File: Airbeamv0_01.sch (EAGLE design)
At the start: 86 parts

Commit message: did Dave's final updates
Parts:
- removed FAN_MOS-N1: DNP, Airbeam:MOSFET
- removed UC_F1: MH2029-300Y, wuerth-elektronik:WE-CBF_0805
- added CA_FB1: FERITE_BEAD, Airbeam:FERITE_BEAD
- added U$1: MOSFET-N, Airbeam:MOSFET-N
- U_FB1: value U_FB1 -> FERITE_BEAD; device wuerth-elektronik:WE-CBF_0805 -> Airbeam:FERITE_BEAD; PARTNO MH2029-300Y -> MH2029-300YCT-ND
- U_FB2: value U_FB2 -> FERITE_BEAD; device wuerth-elektronik:WE-CBF_0805 -> Airbeam:FERITE_BEAD; PARTNO MH2029-300Y -> MH2029-300YCT-ND
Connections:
- net +3V3: now also U$1.P$2; no longer FAN_MOS-N1.P$2
- net +5V: now also U_FB2.P$1; no longer UC_F1.1
- net AVCC: now also U_FB2.P$2; no longer UC_F1.2
- net D5*/FAN_CONTROL: now also U$1.P$1; no longer FAN_MOS-N1.P$1
- net GND: now also CA_FB1.P$1, U_FB1.P$1; no longer U_FB1.2, U_FB2.2
- net N$7: now also CA_FB1.P$2; no longer U_FB1.1
- net UGND: now also U_FB1.P$2; no longer U_FB2.1
- net VFAN: now also U$1.P$3; no longer FAN_MOS-N1.P$3
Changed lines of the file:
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@@
 <attribute name="PARTNO" value="CG0603MLC-05E"/>
-</part>
-<part name="U_FB2" library="wuerth-elektronik" deviceset="WE-CBF" device="_0805" value="U_FB2">
-<attribute name="PARTNO" value="MH2029-300Y"/>
 </part>
 <part name="U$25" library="MyPOW" deviceset="VUSB" device=""/>
 <part name="SUPPLY2" library="supply2" deviceset="GND1" device="" value="UGND"/>
-<part name="UC_F1" library="wuerth-elektronik" deviceset="WE-CBF" device="_0805" value="MH2029-300Y">
-<attribute name="PARTNO" value="MH2029-300Y"/>
-</part>
 <part name="UC_C2" library="SparkFun-Passives" deviceset="CAP" device="0603-CAP" value="100n">
 <attribute name="PARTNO" value="C1608X7R1E104K080AA"/>
@@
 <attribute name="PARTNO" value="RC0603JR-0710KL"/>
 </part>
-<part name="FAN_MOS-N1" library="Airbeam" deviceset="MOSFET" device="" value="DNP">
-<attribute name="PARTNO" value="IRLML2246TRPBF "/>
-</part>
 <part name="VR_R4" library="SparkFun-Resistors" deviceset="RESISTOR" device="0603" value="0">
 <attribute name="PARTNO" value="RC0603JR-070RL"/>
@@
 <attribute name="PARTNO" value="CG0603MLC-05E"/>
 </part>
-<part name="U_FB1" library="wuerth-elektronik" deviceset="WE-CBF" device="_0805" value="U_FB1">
-<attribute name="PARTNO" value="MH2029-300Y"/>
-</part>
 <part name="GND5" library="supply1" deviceset="GND" device=""/>
 <part name="DUST_SENSOR" library="Airbeam" deviceset="PART_OFFBOARD" device="" value="OFF_BOARD">
@@
 </part>
 <part name="GND47" library="supply1" deviceset="GND" device=""/>
+<part name="U_FB1" library="Airbeam" deviceset="FERITE_BEAD" device="">
+<attribute name="PARTNO" value="MH2029-300YCT-ND "/>
+</part>
+<part name="CA_FB1" library="Airbeam" deviceset="FERITE_BEAD" device="">
+<attribute name="PARTNO" value="MH2029-300YCT-ND "/>
+</part>
+<part name="U_FB2" library="Airbeam" deviceset="FERITE_BEAD" device="">
+<attribute name="PARTNO" value="MH2029-300YCT-ND "/>
+</part>
+<part name="U$1" library="Airbeam" deviceset="MOSFET-N" device=""/>
 </parts>
 <sheets>
@@
 <attribute name="PARTNO" x="-86.36" y="-68.58" size="1.778" layer="96" display="off"/>
 </instance>
-<instance part="U_FB2" gate="G$1" x="-129.54" y="-53.34" rot="R180">
-<attribute name="PARTNO" x="-129.54" y="-53.34" size="1.778" layer="96" display="off"/>
-</instance>
 <instance part="U$25" gate="G$1" x="-38.1" y="66.04"/>
 <instance part="SUPPLY2" gate="G$1" x="-53.34" y="38.1"/>
-<instance part="UC_F1" gate="G$1" x="-50.8" y="101.6">
-<attribute name="PARTNO" x="-50.8" y="101.6" size="1.778" layer="96" display="off"/>
-</instance>
 <instance part="UC_C2" gate="G$1" x="-40.64" y="134.62">
 <attribute name="PARTNO" x="-40.64" y="134.62" size="1.778" layer="96" display="off"/>
@@
 <attribute name="PARTNO" x="269.24" y="91.44" size="1.778" layer="96" rot="R180" display="off"/>
 </instance>
-<instance part="FAN_MOS-N1" gate="G$1" x="-96.52" y="-162.56" rot="R270">
-<attribute name="PARTNO" x="-96.52" y="-162.56" size="1.778" layer="96" rot="R270" display="off"/>
-</instance>
 <instance part="VR_R4" gate="G$1" x="-96.52" y="-172.72">
 <attribute name="PARTNO" x="-96.52" y="-172.72" size="1.778" layer="96" display="off"/>
@@
 <attribute name="PARTNO" x="-149.86" y="-205.74" size="1.778" layer="96" rot="R270" display="off"/>
 </instance>
-<instance part="U_FB1" gate="G$1" x="-149.86" y="-218.44" rot="R180">
-<attribute name="PARTNO" x="-149.86" y="-218.44" size="1.778" layer="96" display="off"/>
-</instance>
 <instance part="GND5" gate="1" x="-175.26" y="-193.04" rot="R270"/>
 <instance part="DUST_SENSOR" gate="G$1" x="238.76" y="-5.08">
@@
 </instance>
 <instance part="GND47" gate="1" x="119.38" y="-104.14"/>
+<instance part="U_FB1" gate="G$1" x="-129.54" y="-55.88" rot="R90">
+<attribute name="PARTNO" x="-129.54" y="-55.88" size="1.778" layer="96" rot="R90" display="off"/>
+</instance>
+<instance part="CA_FB1" gate="G$1" x="-149.86" y="-220.98" rot="R90">
+<attribute name="PARTNO" x="-149.86" y="-220.98" size="1.778" layer="96" rot="R90" display="off"/>
+</instance>
+<instance part="U_FB2" gate="G$1" x="-50.8" y="104.14" rot="R90">
+<attribute name="PARTNO" x="-50.8" y="104.14" size="1.778" layer="96" rot="R90" display="off"/>
+</instance>
+<instance part="U$1" gate="G$1" x="-96.52" y="-162.56" rot="R270"/>
 </instances>
 <busses>
@@
 <wire x1="-27.94" y1="106.68" x2="-58.42" y2="106.68" width="0.1524" layer="91"/>
 <wire x1="-58.42" y1="106.68" x2="-58.42" y2="104.14" width="0.1524" layer="91"/>
-<wire x1="-58.42" y1="104.14" x2="-55.88" y2="104.14" width="0.1524" layer="91"/>
 <wire x1="-58.42" y1="104.14" x2="-58.42" y2="101.6" width="0.1524" layer="91"/>
 <wire x1="-58.42" y1="101.6" x2="-27.94" y2="101.6" width="0.1524" layer="91"/>
@@
 <junction x="-27.94" y="127"/>
 <junction x="-58.42" y="104.14"/>
-<pinref part="UC_F1" gate="G$1" pin="1"/>
 <pinref part="U_MEGA32U-Q" gate="G$1" pin="UVCC"/>
 <pinref part="U_MEGA32U-Q" gate="G$1" pin="VCC"/>
@@
 <pinref part="UC_C8" gate="G$1" pin="1"/>
 <junction x="-15.24" y="127"/>
+<pinref part="U_FB2" gate="G$1" pin="P$1"/>
+<wire x1="-53.34" y1="104.14" x2="-58.42" y2="104.14" width="0.1524" layer="91"/>
 </segment>
 <segment>
@@
 <pinref part="BT_C2" gate="G$1" pin="1"/>
 <wire x1="38.1" y1="-134.62" x2="38.1" y2="-139.7" width="0.1524" layer="91"/>
+<junction x="38.1" y="-139.7"/>
 </segment>
 <segment>
@@
 <wire x1="-86.36" y1="-83.82" x2="-96.52" y2="-83.82" width="0.1524" layer="91"/>
 <wire x1="-86.36" y1="-73.66" x2="-86.36" y2="-83.82" width="0.1524" layer="91"/>
-<wire x1="-134.62" y1="-55.88" x2="-144.78" y2="-55.88" width="0.1524" layer="91"/>
+<wire x1="-132.08" y1="-55.88" x2="-144.78" y2="-55.88" width="0.1524" layer="91"/>
 <wire x1="-144.78" y1="-55.88" x2="-144.78" y2="-48.26" width="0.1524" layer="91"/>
 <wire x1="-144.78" y1="-48.26" x2="-144.78" y2="-40.64" width="0.1524" layer="91"/>
@@
 <label x="-142.24" y="-55.88" size="1.778" layer="95"/>
 <pinref part="U_Z1" gate="G$1" pin="2"/>
-<pinref part="U_FB2" gate="G$1" pin="2"/>
 <pinref part="U_Z2" gate="G$1" pin="2"/>
 <pinref part="GND2" gate="1" pin="GND"/>
@@
 <junction x="-127" y="-27.94"/>
 <junction x="-129.54" y="-27.94"/>
+<pinref part="U_FB1" gate="G$1" pin="P$1"/>
 </segment>
 <segment>
@@
 <pinref part="U_Z3" gate="G$1" pin="2"/>
 <wire x1="-167.64" y1="-167.64" x2="-154.94" y2="-167.64" width="0.1524" layer="91"/>
-<pinref part="U_FB1" gate="G$1" pin="2"/>
-<wire x1="-154.94" y1="-220.98" x2="-167.64" y2="-220.98" width="0.1524" layer="91"/>
+<wire x1="-152.4" y1="-220.98" x2="-167.64" y2="-220.98" width="0.1524" layer="91"/>
 <wire x1="-167.64" y1="-220.98" x2="-167.64" y2="-205.74" width="0.1524" layer="91"/>
 <pinref part="GND5" gate="1" pin="GND"/>
@@
 <junction x="-167.64" y="-180.34"/>
 <junction x="-167.64" y="-205.74"/>
+<pinref part="CA_FB1" gate="G$1" pin="P$1"/>
 </segment>
 <segment>
@@
 <pinref part="VR_R4" gate="G$1" pin="1"/>
 <wire x1="-101.6" y1="-172.72" x2="-101.6" y2="-162.56" width="0.1524" layer="91"/>
-<pinref part="FAN_MOS-N1" gate="G$1" pin="P$2"/>
 <wire x1="-101.6" y1="-162.56" x2="-99.06" y2="-162.56" width="0.1524" layer="91"/>
 <wire x1="-101.6" y1="-162.56" x2="-106.68" y2="-162.56" width="0.1524" layer="91"/>
@@
 <pinref part="+3V4" gate="G$1" pin="+3V3"/>
 <junction x="-101.6" y="-162.56"/>
+<pinref part="U$1" gate="G$1" pin="P$2"/>
 </segment>
 <segment>
@@
 </segment>
 <segment>
-<wire x1="-124.46" y1="-55.88" x2="-111.76" y2="-55.88" width="0.1524" layer="91"/>
+<wire x1="-127" y1="-55.88" x2="-111.76" y2="-55.88" width="0.1524" layer="91"/>
 <wire x1="-111.76" y1="-55.88" x2="-111.76" y2="-43.18" width="0.1524" layer="91"/>
 <junction x="-111.76" y="-55.88"/>
 <label x="-119.38" y="-55.88" size="1.778" layer="95"/>
-<pinref part="U_FB2" gate="G$1" pin="1"/>
 <pinref part="SUPPLY1" gate="G$1" pin="GND1"/>
 <pinref part="CON_USB" gate="G$1" pin="T5"/>
 <wire x1="-111.76" y1="-43.18" x2="-121.92" y2="-43.18" width="0.1524" layer="91"/>
+<pinref part="U_FB1" gate="G$1" pin="P$2"/>
 </segment>
 </net>
@@
 </segment>
 <segment>
-<pinref part="FAN_MOS-N1" gate="G$1" pin="P$1"/>
 <wire x1="-96.52" y1="-154.94" x2="-96.52" y2="-160.02" width="0.1524" layer="91"/>
 <label x="-96.52" y="-154.94" size="1.778" layer="95"/>
+<pinref part="U$1" gate="G$1" pin="P$1"/>
 </segment>
 <segment>
@@
 <net name="AVCC" class="0">
 <segment>
-<wire x1="-45.72" y1="104.14" x2="-40.64" y2="104.14" width="0.1524" layer="91"/>
+<wire x1="-48.26" y1="104.14" x2="-40.64" y2="104.14" width="0.1524" layer="91"/>
 <wire x1="-40.64" y1="104.14" x2="-12.7" y2="104.14" width="0.1524" layer="91"/>
 <wire x1="-12.7" y1="104.14" x2="-7.62" y2="104.14" width="0.1524" layer="91"/>
@@
 <junction x="-12.7" y="104.14"/>
 <label x="-40.64" y="104.14" size="1.778" layer="95"/>
-<pinref part="UC_F1" gate="G$1" pin="2"/>
 <pinref part="U_MEGA32U-Q" gate="G$1" pin="AVCC1"/>
 <pinref part="U_MEGA32U-Q" gate="G$1" pin="AVCC"/>
 <pinref part="UC_C5" gate="G$1" pin="1"/>
+<pinref part="U_FB2" gate="G$1" pin="P$2"/>
 </segment>
 <segment>
@@
 <net name="VFAN" class="0">
 <segment>
-<pinref part="FAN_MOS-N1" gate="G$1" pin="P$3"/>
 <wire x1="-93.98" y1="-162.56" x2="-91.44" y2="-162.56" width="0.1524" layer="91"/>
 <pinref part="VR_R4" gate="G$1" pin="2"/>
@@
 <pinref part="CON_FAN" gate="G$1" pin="VCC"/>
 <junction x="-91.44" y="-162.56"/>
+<pinref part="U$1" gate="G$1" pin="P$3"/>
 </segment>
 </net>
@@
 <pinref part="CON_ADDON" gate="G$1" pin="P$5"/>
 <wire x1="-121.92" y1="-144.78" x2="-121.92" y2="-220.98" width="0.1524" layer="91"/>
-<pinref part="U_FB1" gate="G$1" pin="1"/>
-<wire x1="-121.92" y1="-220.98" x2="-144.78" y2="-220.98" width="0.1524" layer="91"/>
-</segment>
-</net>
+<wire x1="-121.92" y1="-220.98" x2="-147.32" y2="-220.98" width="0.1524" layer="91"/>
+<pinref part="CA_FB1" gate="G$1" pin="P$2"/>
+</segment>
+</net>

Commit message: updated per email
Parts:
- removed U_FUSE: 1.8A, SparkFun-PowerIC:PTCSMD-W
- added U_C3: 10uF, SparkFun-Passives:CAP0805
- added U_C4: 100nF, SparkFun-Passives:CAP0603-CAP
- added U_ILIM: USB-OVERCURRENT, Airbeam:USB-OVERCURRENT
- added U_R3: 10k, SparkFun-Passives:RESISTOR0603-RES
- added VR_C1: DNP, Airbeam:CAP_POL120UF
- added VR_FUSE: PTCSMD-W, SparkFun-PowerIC:PTCSMD-W
- VR_D1: value DIODE -> DIODESOD123; device Airbeam:DIODE -> Airbeam:DIODESOD123
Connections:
- new net N$5: VR_FUSE.1, VR_MOS-P1.P$3, VR_R3.2
- new net N$8: U_ILIM.FLG, U_R3.1
- net GND: now also VR_C1.-
- net UGND: now also U_C3.2, U_C4.2, U_ILIM.EN, U_ILIM.GND
- net VREG_IN: now also VR_C1.+, VR_FUSE.2; no longer VR_MOS-P1.P$3, VR_R3.2
- net VUSB: now also U_ILIM.OUT1, U_ILIM.OUT2, U_R3.2; no longer U_FUSE.2
- net XUSB: now also U_C3.1, U_C4.1, U_ILIM.IN1, U_ILIM.IN2; no longer U_FUSE.1
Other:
- moved on the sheet: 3_3V_FAN_COPOL, CON_BAT, DUST_SENSOR, LED_CH, LION_BATTERY, R_LED_CH, UR_C1, UR_R2, U_C1, U_C2, U_VR3, U_VR5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

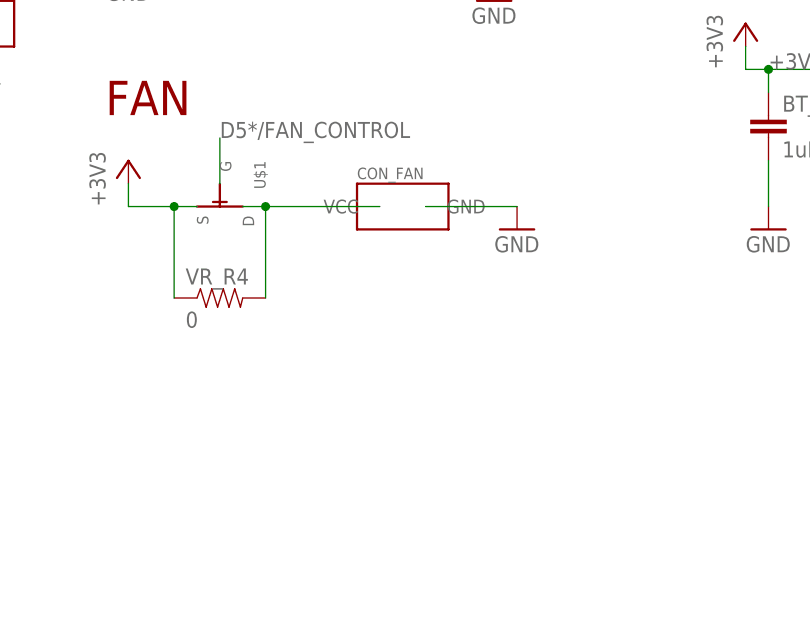
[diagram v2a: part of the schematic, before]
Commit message: added fan connector
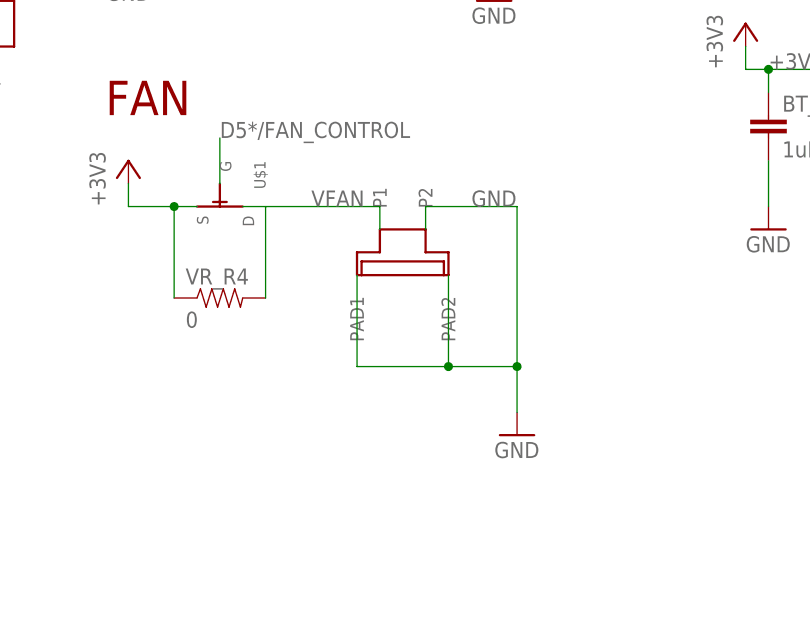
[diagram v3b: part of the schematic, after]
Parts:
- removed CON_FAN: FAN, Airbeam:FAN
- added U$2: SUR_2PIN, Airbeam:SUR_2PIN
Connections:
- net GND: now also U$2.P2, U$2.PAD1, U$2.PAD2; no longer CON_FAN.GND
- net VFAN: now also U$2.P1; no longer CON_FAN.VCC
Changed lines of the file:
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@@
 </part>
 <part name="+3V4" library="supply1" deviceset="+3V3" device=""/>
-<part name="CON_FAN" library="Airbeam" deviceset="FAN" device="">
-<attribute name="PARTNO" value="22-05-7025"/>
-</part>
 <part name="GND14" library="supply1" deviceset="GND" device=""/>
 <part name="R_LED_BT" library="SparkFun-Passives" deviceset="RESISTOR" device="0603-RES" value="1.4k">
@@
 <part name="GND48" library="supply1" deviceset="GND" device=""/>
 <part name="VR_FUSE" library="SparkFun-PowerIC" deviceset="PTC" device="SMD-W"/>
+<part name="U$2" library="Airbeam" deviceset="SUR_2PIN" device=""/>
 </parts>
 <sheets>
@@
 </instance>
 <instance part="+3V4" gate="G$1" x="-106.68" y="-157.48"/>
-<instance part="CON_FAN" gate="G$1" x="-76.2" y="-162.56">
-<attribute name="PARTNO" x="-76.2" y="-162.56" size="1.778" layer="96" display="off"/>
-</instance>
-<instance part="GND14" gate="1" x="-63.5" y="-165.1"/>
+<instance part="GND14" gate="1" x="-63.5" y="-187.96"/>
 <instance part="R_LED_BT" gate="G$1" x="76.2" y="-134.62" rot="R90">
 <attribute name="PARTNO" x="76.2" y="-134.62" size="1.778" layer="96" rot="R90" display="off"/>
@@
 <instance part="GND48" gate="1" x="147.32" y="-33.02"/>
 <instance part="VR_FUSE" gate="G$1" x="104.14" y="-22.86"/>
+<instance part="U$2" gate="G$1" x="-76.2" y="-167.64"/>
 </instances>
 <busses>
@@
 </segment>
 <segment>
-<pinref part="CON_FAN" gate="G$1" pin="GND"/>
-<wire x1="-73.66" y1="-162.56" x2="-63.5" y2="-162.56" width="0.1524" layer="91"/>
-<pinref part="GND14" gate="1" pin="GND"/>
-</segment>
-<segment>
 <pinref part="UBT" gate="G$1" pin="P$2"/>
 <wire x1="-15.24" y1="-121.92" x2="-30.48" y2="-121.92" width="0.1524" layer="91"/>
@@
 <wire x1="147.32" y1="-27.94" x2="147.32" y2="-30.48" width="0.1524" layer="91"/>
 <pinref part="GND48" gate="1" pin="GND"/>
+</segment>
+<segment>
+<pinref part="U$2" gate="G$1" pin="P2"/>
+<pinref part="GND14" gate="1" pin="GND"/>
+<wire x1="-73.66" y1="-165.1" x2="-73.66" y2="-162.56" width="0.1524" layer="91"/>
+<wire x1="-73.66" y1="-162.56" x2="-63.5" y2="-162.56" width="0.1524" layer="91"/>
+<wire x1="-63.5" y1="-162.56" x2="-63.5" y2="-180.34" width="0.1524" layer="91"/>
+<pinref part="U$2" gate="G$1" pin="PAD1"/>
+<wire x1="-63.5" y1="-180.34" x2="-63.5" y2="-185.42" width="0.1524" layer="91"/>
+<wire x1="-81.28" y1="-170.18" x2="-81.28" y2="-180.34" width="0.1524" layer="91"/>
+<wire x1="-81.28" y1="-180.34" x2="-71.12" y2="-180.34" width="0.1524" layer="91"/>
+<pinref part="U$2" gate="G$1" pin="PAD2"/>
+<wire x1="-71.12" y1="-180.34" x2="-71.12" y2="-170.18" width="0.1524" layer="91"/>
+<wire x1="-71.12" y1="-180.34" x2="-63.5" y2="-180.34" width="0.1524" layer="91"/>
+<junction x="-71.12" y="-180.34"/>
+<junction x="-63.5" y="-180.34"/>
+<label x="-68.58" y="-162.56" size="1.778" layer="95"/>
 </segment>
 </net>
@@
 <pinref part="VR_R4" gate="G$1" pin="2"/>
 <wire x1="-91.44" y1="-162.56" x2="-91.44" y2="-172.72" width="0.1524" layer="91"/>
+<pinref part="U$1" gate="G$1" pin="P$3"/>
+<pinref part="U$2" gate="G$1" pin="P1"/>
 <wire x1="-91.44" y1="-162.56" x2="-78.74" y2="-162.56" width="0.1524" layer="91"/>
-<pinref part="CON_FAN" gate="G$1" pin="VCC"/>
-<junction x="-91.44" y="-162.56"/>
-<pinref part="U$1" gate="G$1" pin="P$3"/>
-</segment>
-</net>
+<wire x1="-78.74" y1="-162.56" x2="-78.74" y2="-165.1" width="0.1524" layer="91"/>
+<label x="-86.36" y="-162.56" size="1.778" layer="95"/>
+</segment>
+</net>

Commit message: Final version! We are ordering this one!
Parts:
- CA_FB1, U_FB1, U_FB2: PARTNO MH2029-300YCT-ND -> MH2029-300Y
- CON_ADDON: PARTNO PPTC051LGBN-RC -> 950505-5002-AR
- VR_FUSE: value PTCSMD-W -> 1A; PARTNO (none) -> 0ZCJ0100FF2E
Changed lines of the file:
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@@
 <part name="GND17" library="supply1" deviceset="GND" device=""/>
 <part name="CON_ADDON" library="Airbeam" deviceset="CON_1X5" device="2MM">
-<attribute name="PARTNO" value="PPTC051LGBN-RC "/>
+<attribute name="PARTNO" value="950505-5002-AR"/>
 </part>
 <part name="P+5" library="supply1" deviceset="+5V" device=""/>
@@
 <part name="GND47" library="supply1" deviceset="GND" device=""/>
 <part name="U_FB1" library="Airbeam" deviceset="FERITE_BEAD" device="">
-<attribute name="PARTNO" value="MH2029-300YCT-ND "/>
+<attribute name="PARTNO" value="MH2029-300Y"/>
 </part>
 <part name="CA_FB1" library="Airbeam" deviceset="FERITE_BEAD" device="">
-<attribute name="PARTNO" value="MH2029-300YCT-ND "/>
+<attribute name="PARTNO" value="MH2029-300Y"/>
 </part>
 <part name="U_FB2" library="Airbeam" deviceset="FERITE_BEAD" device="">
-<attribute name="PARTNO" value="MH2029-300YCT-ND "/>
+<attribute name="PARTNO" value="MH2029-300Y"/>
 </part>
 <part name="U$1" library="Airbeam" deviceset="MOSFET-N" device=""/>
@@
 <part name="VR_C1" library="Airbeam" deviceset="CAP_POL" device="120UF" value="DNP"/>
 <part name="GND48" library="supply1" deviceset="GND" device=""/>
-<part name="VR_FUSE" library="SparkFun-PowerIC" deviceset="PTC" device="SMD-W"/>
+<part name="VR_FUSE" library="SparkFun-PowerIC" deviceset="PTC" device="SMD-W" value="1A">
+<attribute name="PARTNO" value="0ZCJ0100FF2E"/>
+</part>
 <part name="U$2" library="Airbeam" deviceset="SUR_2PIN" device=""/>
 </parts>
@@
 <instance part="VR_C1" gate="G$1" x="147.32" y="-25.4"/>
 <instance part="GND48" gate="1" x="147.32" y="-33.02"/>
-<instance part="VR_FUSE" gate="G$1" x="104.14" y="-22.86"/>
+<instance part="VR_FUSE" gate="G$1" x="104.14" y="-22.86">
+<attribute name="PARTNO" x="104.14" y="-22.86" size="1.778" layer="96" display="off"/>
+</instance>
 <instance part="U$2" gate="G$1" x="-76.2" y="-167.64"/>
 </instances>
@@
 <wire x1="-78.74" y1="-162.56" x2="-78.74" y2="-165.1" width="0.1524" layer="91"/>
 <label x="-86.36" y="-162.56" size="1.778" layer="95"/>
-</segment>
-</net>
+<junction x="-91.44" y="-162.56"/>
+</segment>
+</net>
